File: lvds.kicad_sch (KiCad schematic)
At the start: 29 parts, among them J1 Conn_01x22_Female, J3 Conn_01x34_Female, J5 Conn_01x04_Female, U1 SN65DSI83TPAPRQ1, U3 TPS61176RTER

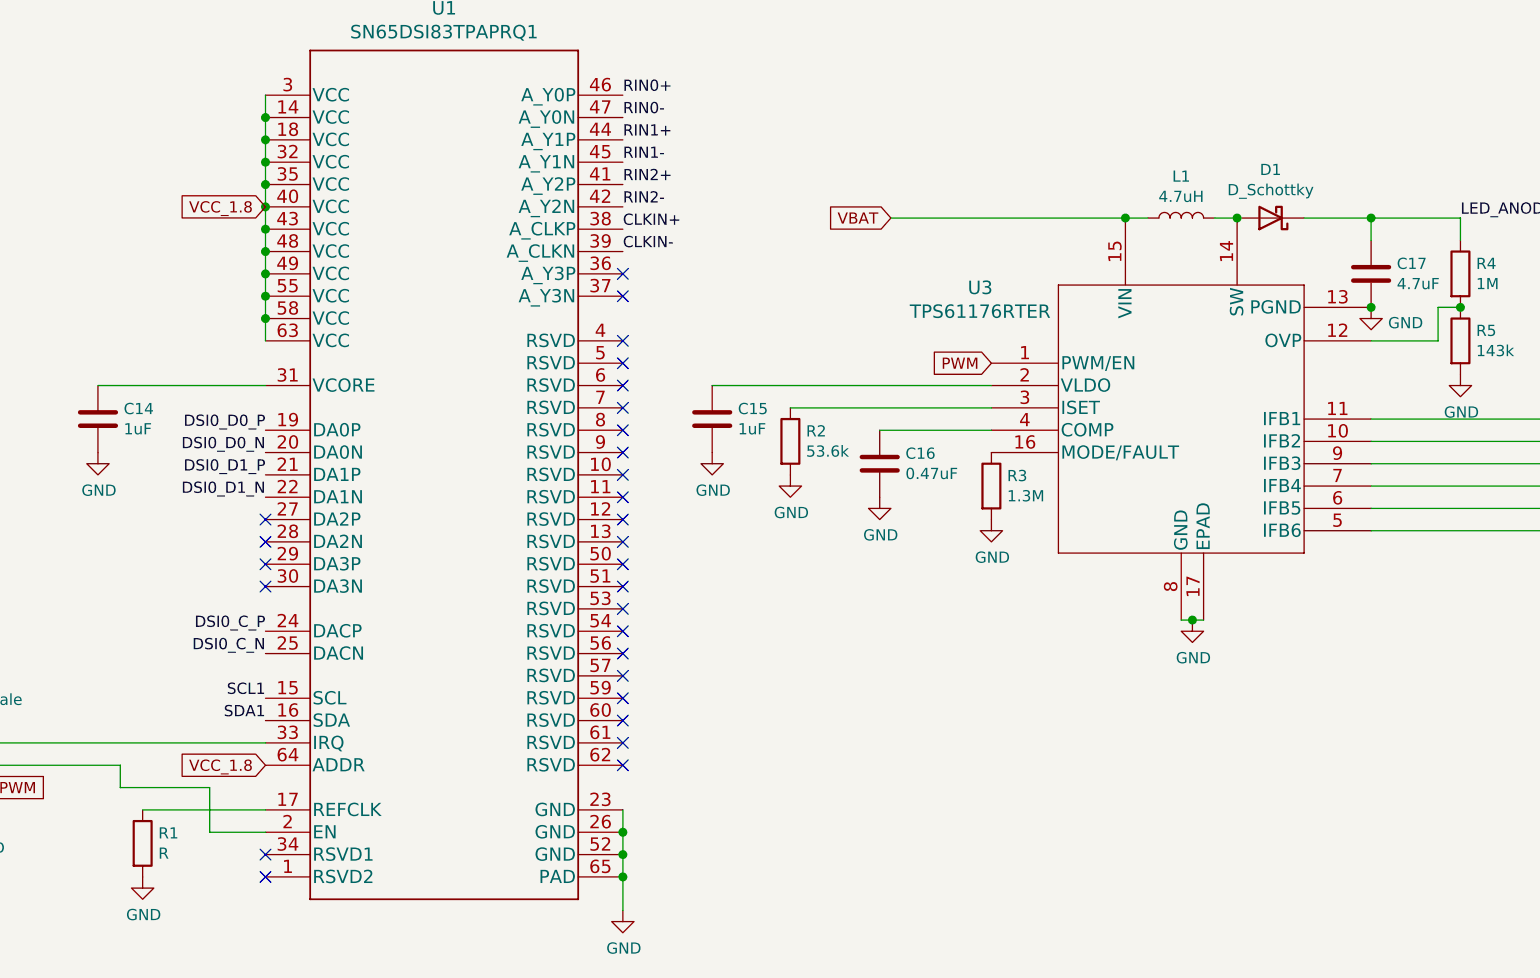
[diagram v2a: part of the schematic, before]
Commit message: Set values for remaining things; choose schottky diode model.
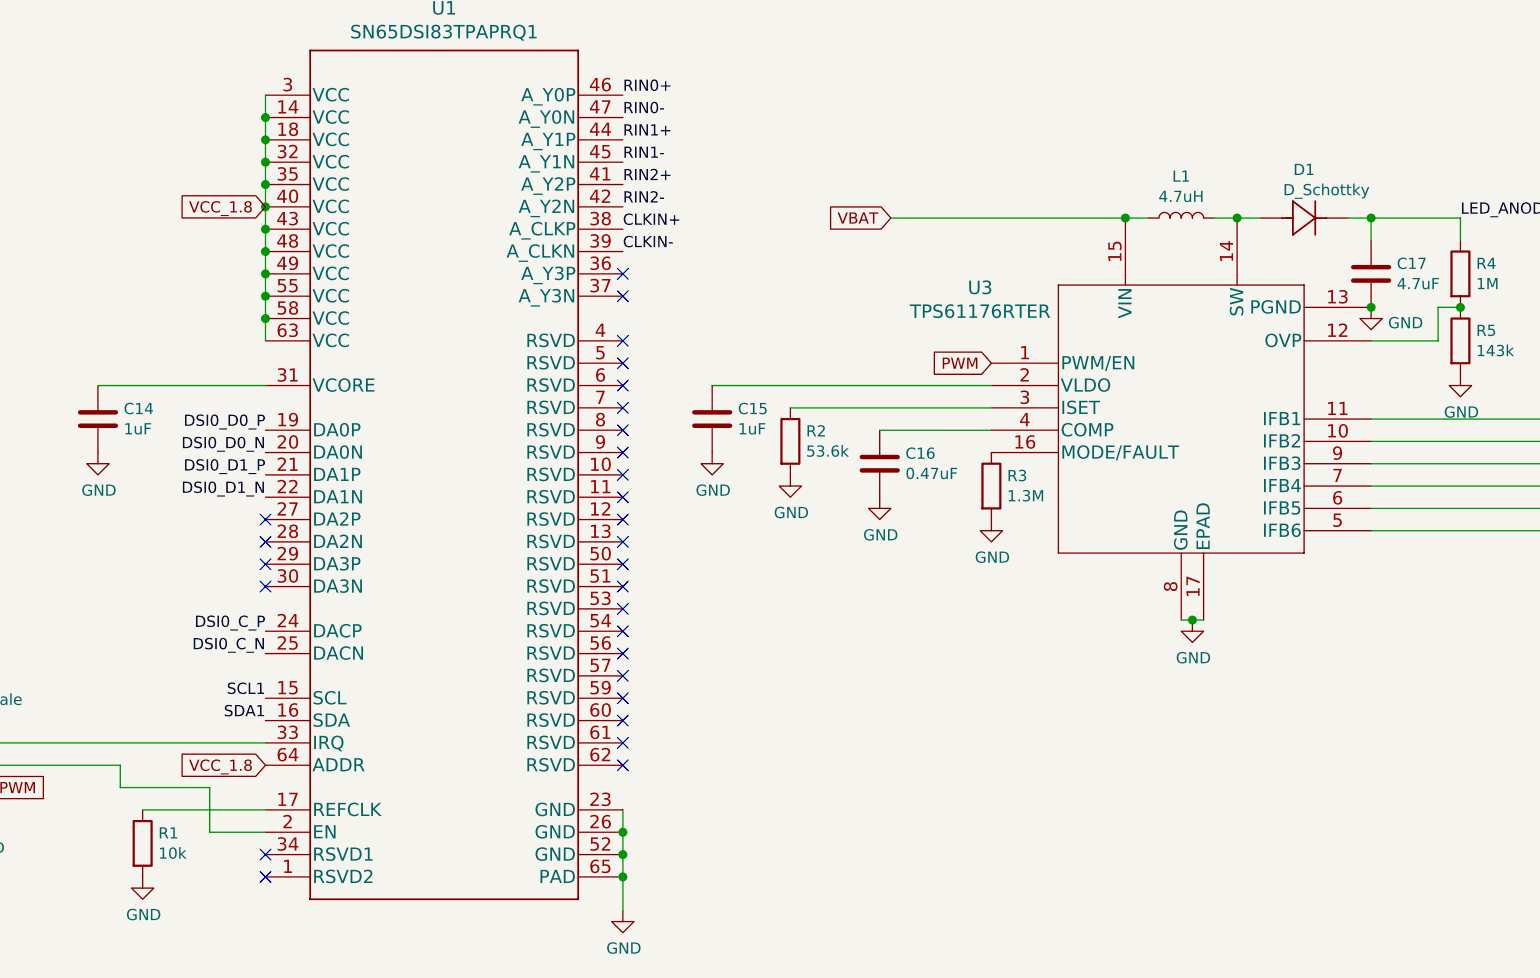
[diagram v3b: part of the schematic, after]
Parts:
- C14, C15, C16, C17: footprint (none) -> Capacitor_SMD:C_0402_1005Metric_Pad0.74x0.62mm_HandSolder
- D1: footprint (none) -> footprints:PMEG4010EPK_315; symbol Device:D_Schottky -> PMEG4010EPK_315:PMEG4010EPK_315
- J5: footprint (none) -> Connector_PinHeader_2.54mm:PinHeader_1x04_P2.54mm_Vertical
- L1: footprint (none) -> Inductor_SMD:L_0603_1608Metric_Pad1.05x0.95mm_HandSolder
- R1: value R -> 10k; footprint (none) -> Resistor_SMD:R_0402_1005Metric_Pad0.72x0.64mm_HandSolder
- R2, R3, R4, R5: footprint (none) -> Resistor_SMD:R_0402_1005Metric_Pad0.72x0.64mm_HandSolder
- U1: footprint PAP0064Q_N -> footprints:SN65DSI83TPAPRQ1
- U3: footprint RTE16_1P66X1P66_TEX -> footprints:TPS61176RTER
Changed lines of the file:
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@@
     (stroke (width 0) (type solid) (color 0 0 0 0))
   )
-  (wire (pts (xy 215.9 64.77) (xy 208.28 64.77))
+  (wire (pts (xy 203.2 64.77) (xy 200.66 64.77))
+    (stroke (width 0) (type solid) (color 0 0 0 0))
+  )
+  (wire (pts (xy 215.9 64.77) (xy 213.36 64.77))
     (stroke (width 0) (type solid) (color 0 0 0 0))
   )
@@
     (property "Reference" "L1" (id 0) (at 194.31 60.0518 90))
     (property "Value" "4.7uH" (id 1) (at 194.31 62.35 90))
-    (property "Footprint" "" (id 2) (at 194.31 64.77 0)
+    (property "Footprint" "Inductor_SMD:L_0603_1608Metric_Pad1.05x0.95mm_HandSolder" (id 2) (at 194.31 64.77 0)
       (effects (font (size 1.27 1.27)) hide)
     )
@@
       (effects (font (size 1.27 1.27)) (justify left))
     )
-    (property "Value" "R" (id 1) (at 77.9781 137.0393 0)
-      (effects (font (size 1.27 1.27)) (justify left))
-    )
-    (property "Footprint" "" (id 2) (at 74.422 135.89 90)
+    (property "Value" "10k" (id 1) (at 77.978 137.039 0)
+      (effects (font (size 1.27 1.27)) (justify left))
+    )
+    (property "Footprint" "Resistor_SMD:R_0402_1005Metric_Pad0.72x0.64mm_HandSolder" (id 2) (at 74.422 135.89 90)
       (effects (font (size 1.27 1.27)) hide)
     )
@@
       (effects (font (size 1.27 1.27)) (justify left))
     )
-    (property "Footprint" "" (id 2) (at 148.082 90.17 90)
+    (property "Footprint" "Resistor_SMD:R_0402_1005Metric_Pad0.72x0.64mm_HandSolder" (id 2) (at 148.082 90.17 90)
       (effects (font (size 1.27 1.27)) hide)
     )
@@
       (effects (font (size 1.27 1.27)) (justify left))
     )
-    (property "Footprint" "" (id 2) (at 170.942 95.25 90)
+    (property "Footprint" "Resistor_SMD:R_0402_1005Metric_Pad0.72x0.64mm_HandSolder" (id 2) (at 170.942 95.25 90)
       (effects (font (size 1.27 1.27)) hide)
     )
@@
       (effects (font (size 1.27 1.27)) (justify left))
     )
-    (property "Footprint" "" (id 2) (at 224.282 71.12 90)
+    (property "Footprint" "Resistor_SMD:R_0402_1005Metric_Pad0.72x0.64mm_HandSolder" (id 2) (at 224.282 71.12 90)
       (effects (font (size 1.27 1.27)) hide)
     )
@@
       (effects (font (size 1.27 1.27)) (justify left))
     )
-    (property "Footprint" "" (id 2) (at 224.282 78.74 90)
+    (property "Footprint" "Resistor_SMD:R_0402_1005Metric_Pad0.72x0.64mm_HandSolder" (id 2) (at 224.282 78.74 90)
       (effects (font (size 1.27 1.27)) hide)
     )
@@
     (pin "2")
   )
-  (symbol (lib_id "Device:D_Schottky") (at 204.47 64.77 180) (unit 1)
-    (in_bom yes) (on_board yes)
-    (property "Reference" "D1" (id 0) (at 204.47 59.2898 0))
-    (property "Value" "D_Schottky" (id 1) (at 204.47 61.5885 0))
-    (property "Footprint" "" (id 2) (at 204.47 64.77 0)
-      (effects (font (size 1.27 1.27)) hide)
-    )
-    (property "Datasheet" "~" (id 3) (at 204.47 64.77 0)
-      (effects (font (size 1.27 1.27)) hide)
-    )
-    (pin "1")
-    (pin "2")
-  )
   (symbol (lib_id "Device:C") (at 25.4 25.4 0) (unit 1)
     (in_bom yes) (on_board yes)
@@
       (effects (font (size 1.27 1.27)) (justify left))
     )
-    (property "Footprint" "" (id 2) (at 72.0852 91.44 0)
+    (property "Footprint" "Capacitor_SMD:C_0402_1005Metric_Pad0.74x0.62mm_HandSolder" (id 2) (at 72.0852 91.44 0)
       (effects (font (size 1.27 1.27)) hide)
     )
@@
       (effects (font (size 1.27 1.27)) (justify left))
     )
-    (property "Footprint" "" (id 2) (at 141.9352 91.44 0)
+    (property "Footprint" "Capacitor_SMD:C_0402_1005Metric_Pad0.74x0.62mm_HandSolder" (id 2) (at 141.9352 91.44 0)
       (effects (font (size 1.27 1.27)) hide)
     )
@@
       (effects (font (size 1.27 1.27)) (justify left))
     )
-    (property "Footprint" "" (id 2) (at 160.9852 96.52 0)
+    (property "Footprint" "Capacitor_SMD:C_0402_1005Metric_Pad0.74x0.62mm_HandSolder" (id 2) (at 160.9852 96.52 0)
       (effects (font (size 1.27 1.27)) hide)
     )
@@
       (effects (font (size 1.27 1.27)) (justify left))
     )
-    (property "Footprint" "" (id 2) (at 216.8652 74.93 0)
+    (property "Footprint" "Capacitor_SMD:C_0402_1005Metric_Pad0.74x0.62mm_HandSolder" (id 2) (at 216.8652 74.93 0)
       (effects (font (size 1.27 1.27)) hide)
     )
@@
     (pin "1")
     (pin "2")
+  )
+  (symbol (lib_id "PMEG4010EPK_315:PMEG4010EPK_315") (at 208.28 64.77 0) (unit 1)
+    (in_bom yes) (on_board yes)
+    (property "Reference" "D1" (id 0) (at 208.28 59.2898 0))
+    (property "Value" "D_Schottky" (id 1) (at 210.82 61.5885 0))
+    (property "Footprint" "footprints:PMEG4010EPK_315" (id 2) (at 213.36 55.626 0)
+      (effects (font (size 1.524 1.524)) hide)
+    )
+    (property "Datasheet" "~" (id 3) (at 203.2 64.77 0)
+      (effects (font (size 1.524 1.524)))
+    )
+    (pin "2")
+    (pin "1")
   )
   (symbol (lib_id "Connector:Conn_01x04_Female") (at 53.34 127 0) (mirror y) (unit 1)
@@
     (property "Reference" "J5" (id 0) (at 56.0324 122.3326 0))
     (property "Value" "Conn_01x04_Female" (id 1) (at 53.492 119.551 0))
-    (property "Footprint" "" (id 2) (at 53.34 127 0)
+    (property "Footprint" "Connector_PinHeader_2.54mm:PinHeader_1x04_P2.54mm_Vertical" (id 2) (at 53.34 127 0)
       (effects (font (size 1.27 1.27)) hide)
     )
@@
       (effects (font (size 1.524 1.524)))
     )
-    (property "Footprint" "RTE16_1P66X1P66_TEX" (id 2) (at 210.82 71.374 0)
+    (property "Footprint" "footprints:TPS61176RTER" (id 2) (at 210.82 71.374 0)
       (effects (font (size 1.524 1.524)) hide)
     )
@@
       (effects (font (size 1.524 1.524)))
     )
-    (property "Footprint" "PAP0064Q_N" (id 2) (at 110.49 95.504 0)
+    (property "Footprint" "footprints:SN65DSI83TPAPRQ1" (id 2) (at 110.49 95.504 0)
       (effects (font (size 1.524 1.524)) hide)
     )

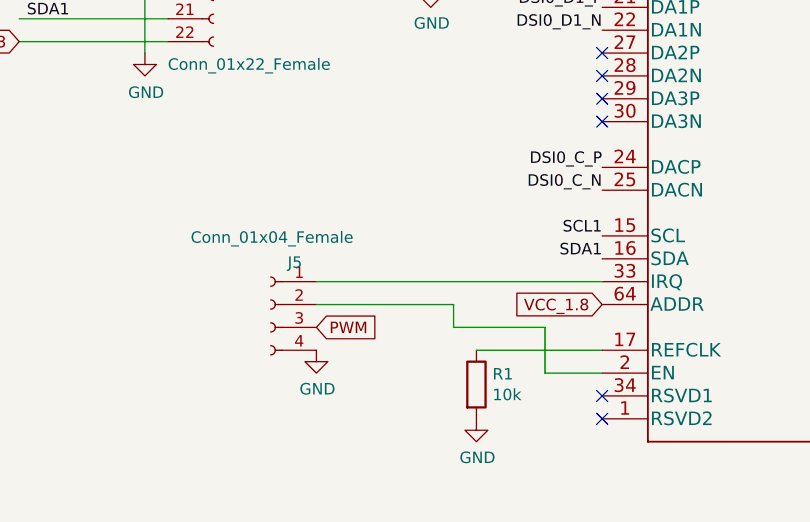
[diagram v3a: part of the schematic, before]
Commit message: rearrange J4 pins to make traces for LDO simpler.
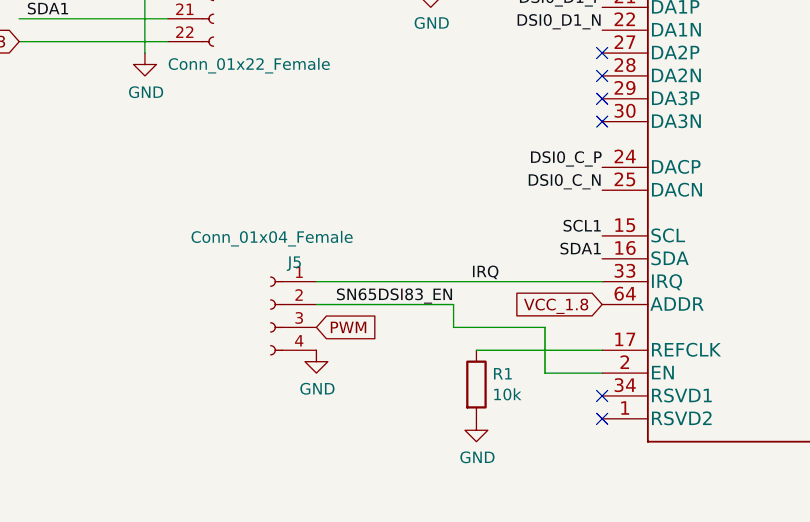
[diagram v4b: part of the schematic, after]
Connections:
- net IRQ: now reaches J5.1 (Pin_1), U1.33 (IRQ)
- net SN65DSI83_EN: now reaches J5.2 (Pin_2), U1.2 (EN)
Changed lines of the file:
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@@
+    (effects (font (size 1.27 1.27)) (justify right bottom))
+  )
+  (label "SN65DSI83_EN" (at 73.66 127 180)
+    (effects (font (size 1.27 1.27)) (justify right bottom))
+  )
+  (label "IRQ" (at 78.74 124.46 180)
     (effects (font (size 1.27 1.27)) (justify right bottom))
   )

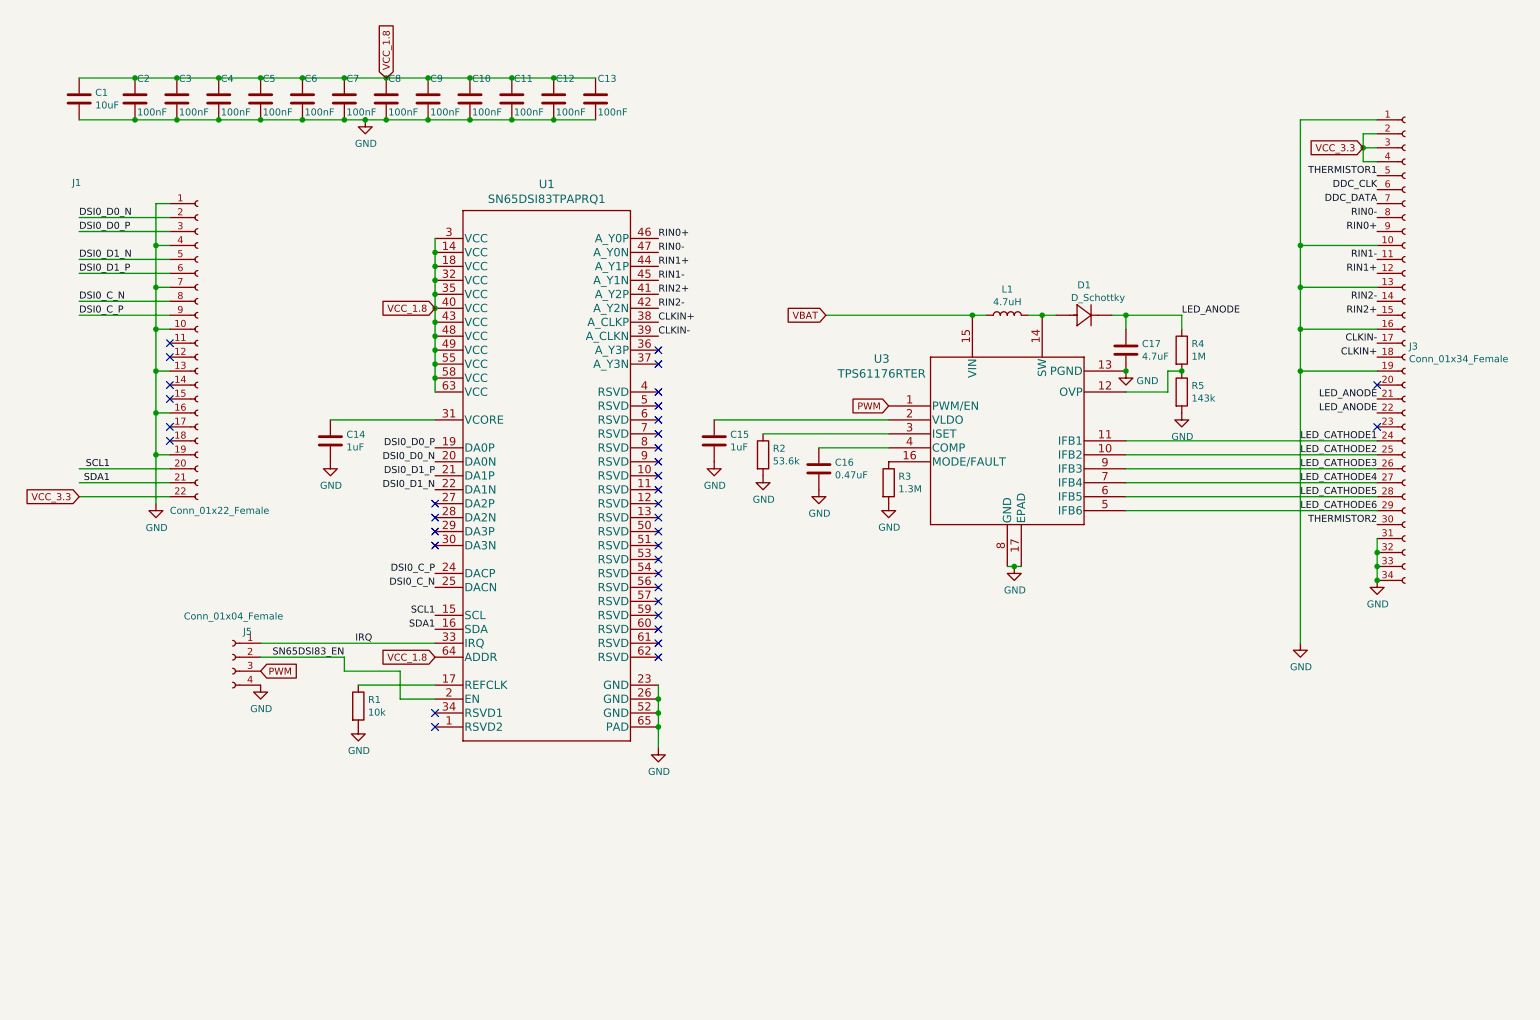
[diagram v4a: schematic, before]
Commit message: Import LVDS schematic as hierarchical sheet. Add level shifters for I2C and EN/IRQ pins.
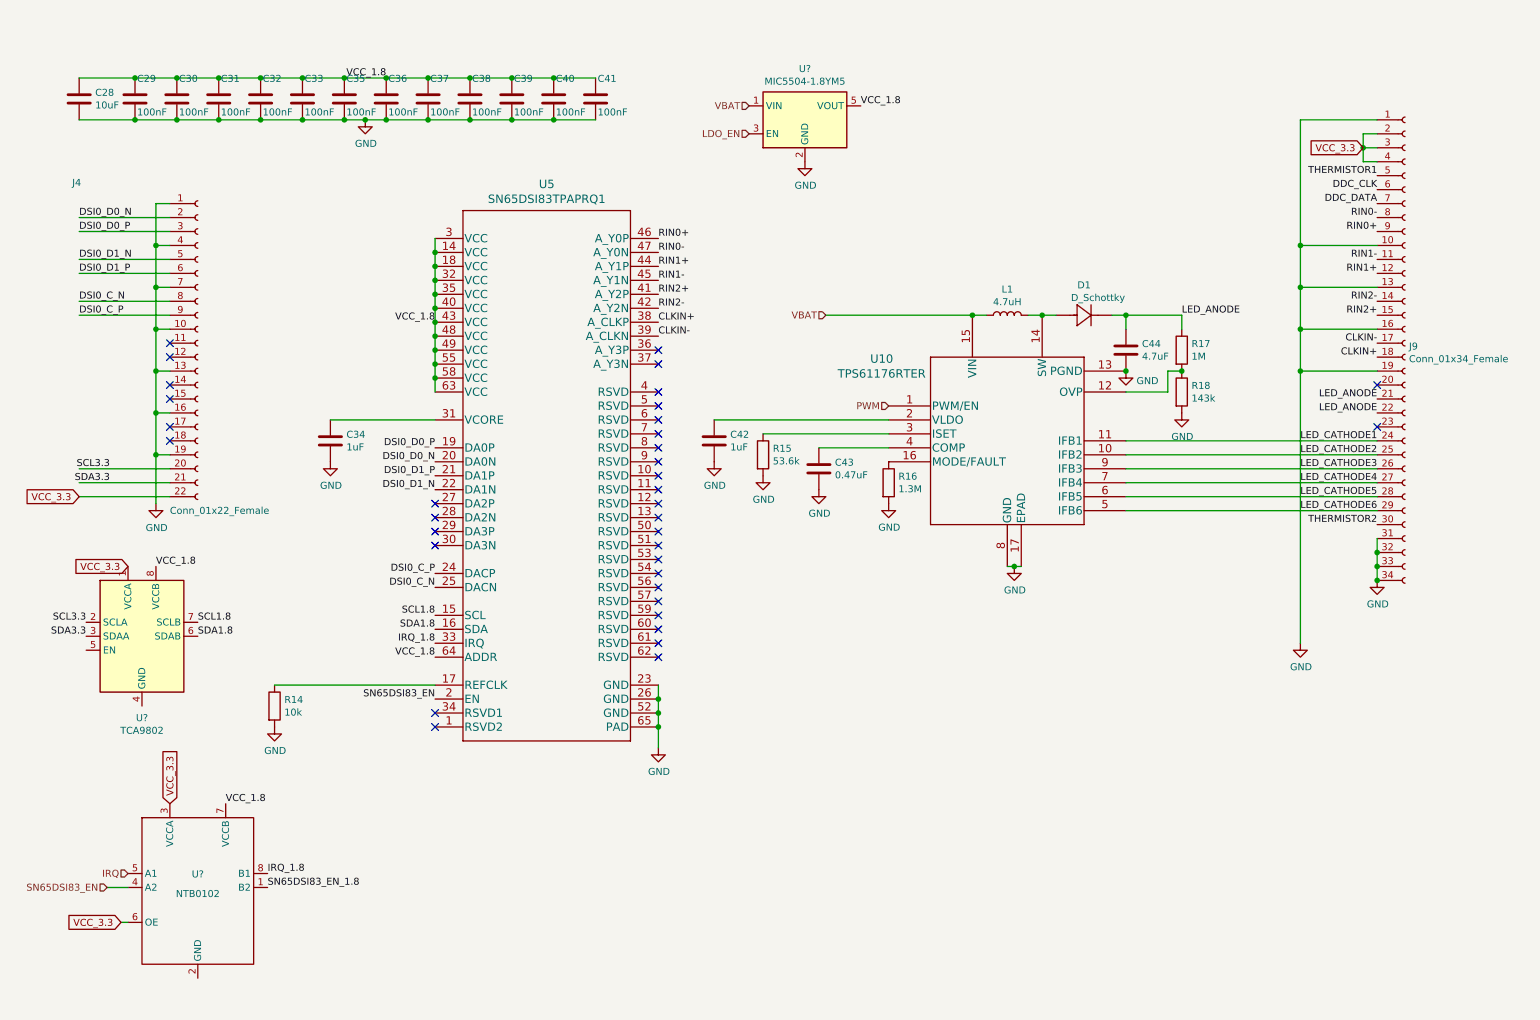
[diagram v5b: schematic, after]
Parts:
- removed J5: Conn_01x04_Female, Connector_PinHeader_2.54mm:PinHeader_1x04_P2.54mm_Vertical, symbol Connector:Conn_01x04_Female
- added U?: TCA9802, Package_SO:VSSOP-8_3.0x3.0mm_P0.65mm, symbol Interface:TCA9802
- added U?: MIC5504-1.8YM5, Package_TO_SOT_SMD:SOT-23-5, symbol Regulator_Linear:MIC5504-1.8YM5
- added U?: NTB0102, symbol NTB0102:NTB0102
- renumbered C1 to C28, C2 to C29, C3 to C30, C4 to C31, C5 to C32, C6 to C33, C14 to C34, C7 to C35, C8 to C36, C9 to C37, C10 to C38, C11 to C39, C12 to C40, C13 to C41, C15 to C42, C16 to C43, C17 to C44, J1 to J4, J3 to J9, R1 to R14, R2 to R15, R3 to R16, R4 to R17, R5 to R18, U3 to U10, U1 to U5
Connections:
- net GND: now also U?.2 (GND)
- net IRQ: now also U?.5 (A1); no longer U5.33 (IRQ)
- net SN65DSI83_EN: now also U?.4 (A2)
- net VBAT: now also U?.1 (VIN)
- net VCC_1.8: now also U?.5 (VOUT), U?.7 (VCCB), U?.8 (VCCB)
- net VCC_3.3: now also U?.1 (VCCA), U?.3 (VCCA), U?.6 (OE)
- net SCL1 renamed SCL1.8
- net SCL1.8: now also U?.7 (SCLB); no longer J4.20 (Pin_20)
- net SDA1 renamed SDA1.8
- net SDA1.8: now also U?.6 (SDAB); no longer J4.21 (Pin_21)
- new net IRQ_1.8: U5.33 (IRQ), U?.8 (B1)
- new net LDO_EN: U?.3 (EN)
- new net SCL3.3: J4.20 (Pin_20), U?.2 (SCLA)
- new net SDA3.3: J4.21 (Pin_21), U?.3 (SDAA)
- new net SN65DSI83_EN_1.8: U?.1 (B2)
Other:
- moved on the sheet: R14
